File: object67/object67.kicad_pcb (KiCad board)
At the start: 2 copper layers, 200 parts, among them IC1 AK4493SEQ, IC2 TAA5242IRGER, IC3 LMK1C1104PWR, IC4 TPA6120A2DWPR, IC5 TPS7A4701RGWT, IC6 TPS7A3301RGWR, J1 SN37A12B, J2 PJ-037A, J3 Power In, J4 216700-0249, J5 216700-0249, J6 Conn_02x08_Odd_Even, U1 RCJ-2223, U10 ADP5070AREZ, U11 TPS62912, U2 OPA1612AxD, U3 OPA1612AxD, U4 OPA1612AxD, U5 RCJ-2223, U6 OPA1612AxD, U7 TPS7A2050PDQNR, U8 TPS7A2033PDQNR, U9 TPS7A2033PDQNR, Y3 ASDLJ-E-49.152MHZ-L-R-T, Y4 ASDLJ-E-45.1584MHz-L-R-T

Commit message: Updated pcb
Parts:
- added R46: 22, Capacitor_SMD:C_0201_0603Metric, F.Cu at (66.9, 97.0)
- moved C76 124.3 mm to (56.6, 142.1)
- moved C77 124.3 mm to (56.6, 144.6)
- moved C85 124.3 mm to (63.4, 159.9)
- moved C86 124.3 mm to (63.4, 162.9)
- moved C87 124.3 mm to (63.4, 165.9)
- moved FB4 124.3 mm to (56.6, 147.1)
- moved IC5 124.3 mm to (62.3, 144.5)
- moved IC6 124.3 mm to (62.3, 151.8)
- moved J4 124.3 mm to (41.3, 168.5)
- moved J5 124.3 mm to (41.3, 173.7)
- moved R41 124.3 mm to (56.6, 149.6)
- moved C59 124.3 mm to (48.6, 142.1)
- moved C60 124.3 mm to (48.6, 144.6)
- moved C61 124.3 mm to (48.6, 147.1)
- moved C62 124.3 mm to (48.6, 149.6)
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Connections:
- C1 pad 2: GNDA -> GND
- C10 pad 2: GNDA -> GND
- C11 pad 2: GNDA -> GND
- C12 pad 2: GNDA -> GND
- C13 pad 2: GNDA -> GND
- C14 pad 2: GNDA -> GND
- C15 pad 2: GNDA -> GND
- C16 pad 2: GNDA -> GND
- C17 pad 2: GNDA -> GND
- C18 pad 2: GNDA -> GND
- C19 pad 2: GNDA -> GND
- C2 pad 2: GNDA -> GND
- C20 pad 2: GNDA -> GND
- C21 pad 2: GNDA -> GND
- C22 pad 1: GNDA -> GND
- C24 pad 2: GNDA -> GND
- C25 pad 2: GNDA -> GND
- C26 pad 2: GNDA -> GND
- C27 pad 2: GNDA -> GND
- C28 pad 1: GNDA -> GND
- C29 pad 1: GNDA -> GND
- C3 pad 2: GNDA -> GND
- C30 pad 2: GNDA -> GND
- C31 pad 2: GNDA -> GND
- C32 pad 1: GNDA -> GND
- C33 pad 1: GNDA -> GND
- C34 pad 2: GNDA -> GND
- C36 pad 2: GNDA -> GND
- C38 pad 2: GNDA -> GND
- C4 pad 2: GNDA -> GND
- C40 pad 2: GNDA -> GND
- C42 pad 2: GNDA -> GND
- C43 pad 1: GNDA -> GND
- C44 pad 2: GNDA -> GND
- C45 pad 1: GNDA -> GND
- C46 pad 2: GNDA -> GND
- C47 pad 1: GNDA -> GND
- C48 pad 2: GNDA -> GND
- C49 pad 1: GNDA -> GND
- C5 pad 2: GNDA -> GND
- C50 pad 2: GNDA -> GND
- C51 pad 1: GNDA -> GND
- C52 pad 2: GNDA -> GND
- C53 pad 1: GNDA -> GND
- C54 pad 1: GNDA -> GND
- C55 pad 1: GNDA -> GND
- C56 pad 1: GNDA -> GND
- C57 pad 1: GNDA -> GND
- C59 pad 2: GNDA -> GND
- C6 pad 2: GNDA -> GND
- C60 pad 2: GNDA -> GND
- C61 pad 2: GNDA -> GND
- C62 pad 2: GNDA -> GND
- C63 pad 2: GNDA -> GND
- C64 pad 2: GNDA -> GND
- C65 pad 2: GNDA -> GND
- C66 pad 2: GNDA -> GND
- C67 pad 2: GNDA -> GND
- C68 pad 2: GNDA -> GND
- C69 pad 2: GNDA -> GND
- C7 pad 2: GNDA -> GND
- C70 pad 2: GNDA -> GND
- C71 pad 1: GNDA -> GND
- C72 pad 1: GNDPWR -> GND
- C73 pad 1: GNDA -> GND
- C74 pad 1: GNDA -> GND
- C75 pad 2: GNDA -> GND
- C76 pad 1: GNDPWR -> GND
- C77 pad 1: GNDPWR -> GND
- C78 pad 1: GNDPWR -> GND
- C79 pad 1: GNDPWR -> GND
- C8 pad 2: GNDA -> GND
- C80 pad 1: GNDPWR -> GND
- C81 pad 1: GNDPWR -> GND
- C82 pad 1: GNDPWR -> GND
- C83 pad 1: GNDPWR -> GND
- C84 pad 1: GNDPWR -> GND
- C85 pad 1: GNDPWR -> GND
- C86 pad 1: GNDPWR -> GND
- C87 pad 1: GNDA -> GND
- C88 pad 2: GNDA -> GND
- C89 pad 2: GNDA -> GND
- C9 pad 2: GNDA -> GND
- C90 pad 2: GNDA -> GND
- C92 pad 1: GNDA -> GND
- C93 pad 2: GNDA -> GND
- C94 pad 2: GNDA -> GND
- C95 pad 2: GNDA -> GND
- C96 pad 2: GNDA -> GND
- C97 pad 2: GNDA -> GND
- H1 pad 1: GNDPWR -> GND
- IC1 pad 12: GNDA -> GND
- IC1 pad 13: GNDA -> GND
- IC1 pad 17: GNDA -> GND
- IC1 pad 18: GNDA -> GND
- IC1 pad 21: GNDA -> GND
- IC1 pad 22: GNDA -> GND
- IC1 pad 24: GNDA -> GND
- IC1 pad 27: GNDA -> GND
- IC1 pad 28: GNDA -> GND
- IC1 pad 31: GNDA -> GND
- IC1 pad 32: GNDA -> GND
- IC1 pad 37: GNDA -> GND
- IC1 pad 39: GNDA -> GND
- IC1 pad 40: GNDA -> GND
- IC1 pad 43: GNDA -> GND
- IC1 pad 45: GNDA -> GND
- IC1 pad 46: MLCK_{DAC} -> Net-(IC1-MCLK)
- IC1 pad 47: GNDA -> GND
- IC2 pad 13: GNDA -> GND
- IC2 pad 19: GNDA -> GND
- IC2 pad 20: GNDA -> GND
- IC2 pad 21: GNDA -> GND
- IC2 pad 22: GNDA -> GND
- IC2 pad 25: GNDA -> GND
- IC2 pad 26: GNDA -> GND
- IC2 pad 27: GNDA -> GND
- IC2 pad 28: GNDA -> GND
- IC2 pad 29: GNDA -> GND
- IC2 pad 5: GNDA -> GND
- IC2 pad 7: GNDA -> GND
- IC2 pad 8: GNDA -> GND
- IC2 pad 9: GNDA -> GND
- IC3 pad 4: GNDA -> GND
- IC4 pad 21: GNDA -> GND
- IC5 pad 21: GNDA -> GND
- IC5 pad 4: GNDA -> GND
- IC5 pad 5: GNDA -> GND
- IC5 pad 7: GNDA -> GND
- IC5 pad 9: GNDA -> GND
- J1 pad S: GNDA -> GND
- J2 pad 1: GNDPWR -> GND
- J3 pad 2: GNDPWR -> GND
- J4 pad 10: GNDA -> GND
- J4 pad 11: GNDA -> GND
- J4 pad 12: GNDA -> GND
- J4 pad 13: GNDA -> GND
- J4 pad 14: GNDA -> GND
- J4 pad 15: GNDA -> GND
- J4 pad 21: GNDA -> GND
- J4 pad 22: GNDA -> GND
- J4 pad 23: GNDA -> GND
- J4 pad 24: GNDA -> GND
- J5 pad 10: GNDA -> GND
- J5 pad 11: GNDA -> GND
- J5 pad 12: GNDA -> GND
- J5 pad 13: GNDA -> GND
- J5 pad 14: GNDA -> GND
- J5 pad 15: GNDA -> GND
- J5 pad 21: GNDA -> GND
- J5 pad 22: GNDA -> GND
- J5 pad 23: GNDA -> GND
- J5 pad 24: GNDA -> GND
- J5 pad 7: GNDA -> GND
- J5 pad 8: GNDA -> GND
- J5 pad 9: GNDA -> GND
- J6 pad 15: GNDA -> GND
- L2 pad 1: GNDPWR -> GND
- R25 pad 1: GNDA -> GND
- R27 pad 1: GNDA -> GND
- R33 pad 1: GNDA -> GND
- R34 pad 1: GNDA -> GND
- R38 pad 1: GNDA -> GND
- R41 pad 1: GNDPWR -> GND
- R43 pad 1: GNDPWR -> GND
- R45 pad 1: GNDA -> GND
- R6 pad 1: GNDA -> GND
- R7 pad 1: GNDA -> GND
- U10 pad 1: GNDPWR -> GND
- U10 pad 15: GNDA -> GND
- U10 pad 21: GNDA -> GND
- U10 pad 4: GNDA -> GND
- U11 pad 4: GNDPWR -> GND
- U11 pad 7: GNDPWR -> GND
- U4 pad 3: GNDA -> GND
- U4 pad 5: GNDA -> GND
- U6 pad 3: GNDA -> GND
- U6 pad 5: GNDA -> GND
- U7 pad 2: GNDA -> GND
- U7 pad 5: GNDA -> GND
- U8 pad 2: GNDA -> GND
- U8 pad 5: GNDA -> GND
- U9 pad 2: GNDA -> GND
- U9 pad 5: GNDA -> GND
- Y3 pad 2: GNDA -> GND
- Y4 pad 2: GNDA -> GND
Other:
- copper layers 2 -> 4

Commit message: More layouts
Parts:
- moved J1 278.7 mm to (303.5, 150.2)
- moved U1 260.2 mm to (302.8, 129.5), turned to -90 degrees
- moved U5 259.3 mm to (303.0, 109.3), turned to -90 degrees
- moved IC4 233.7 mm to (275.5, 150.5)
- moved IC2 227.9 mm to (257.3, 146.7)
- moved U6 225.4 mm to (273.5, 136.3), turned to 90 degrees
- moved U4 224.6 mm to (273.3, 130.1), turned to 90 degrees
- moved U3 224.0 mm to (273.1, 123.8), turned to 90 degrees
- moved U2 223.3 mm to (273.3, 116.6), turned to 90 degrees
- moved IC5 213.4 mm to (272.4, 107.3)
- moved IC6 202.5 mm to (259.9, 107.3)
- moved IC1 202.4 mm to (257.0, 132.3)
- moved J6 200.9 mm to (232.1, 158.0), turned to -90 degrees
- moved IC3 200.0 mm to (244.5, 138.0), turned to 90 degrees
- moved J4 191.0 mm to (229.4, 135.6), turned to 180 degrees
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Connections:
- IC3 pad 3: MLCK_{MCU} -> MLCK_{DAC}
- IC3 pad 8: MLCK_{DAC} -> MLCK_{MCU}
- TP10 pad 1: MLCK_{MCU} -> MLCK_{DAC}
- TP9 pad 1: MLCK_{DAC} -> MLCK_{MCU}

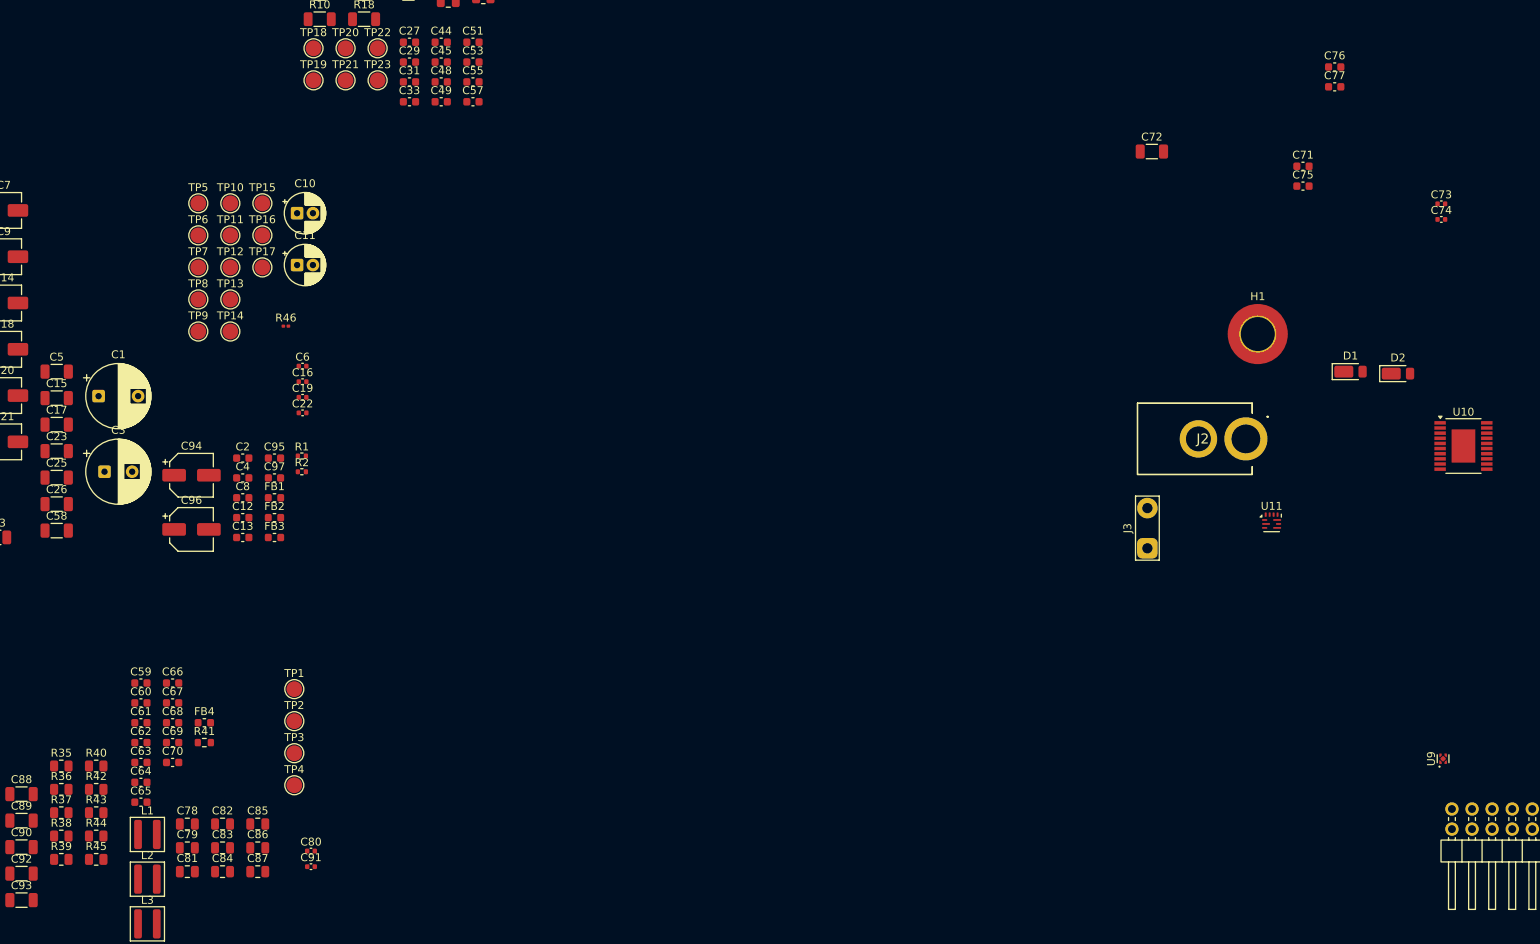
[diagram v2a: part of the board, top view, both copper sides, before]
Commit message: Layout for ADP5070
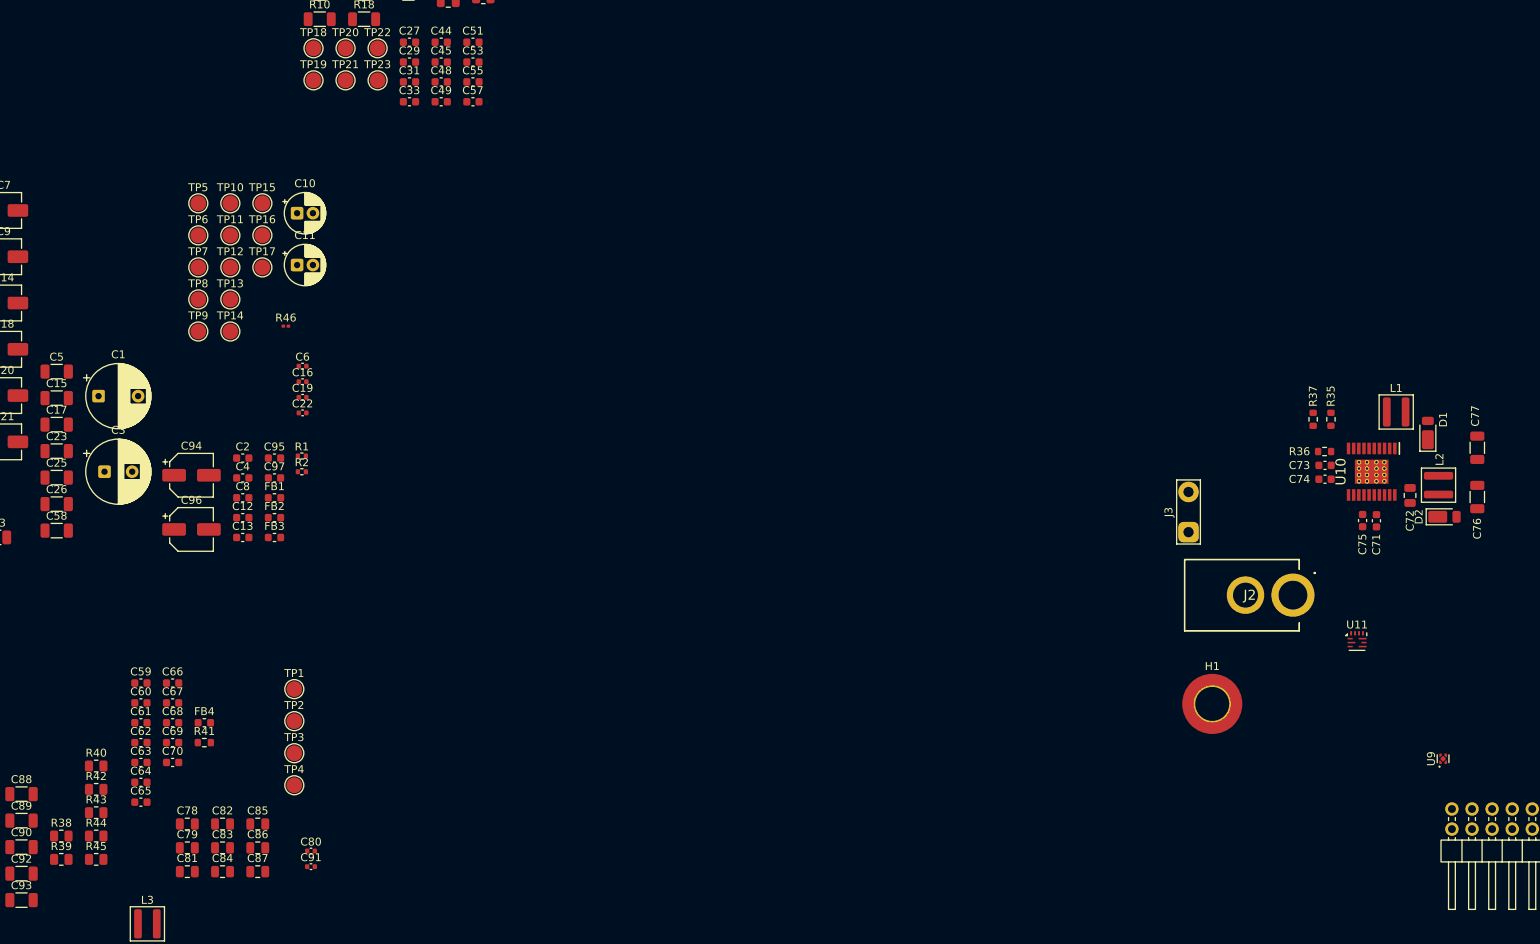
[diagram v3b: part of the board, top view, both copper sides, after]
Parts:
- C72: footprint Capacitor_SMD:C_1206_3216Metric -> Capacitor_SMD:C_0805_2012Metric
- C73, C74: footprint Capacitor_SMD:C_0402_1005Metric -> Capacitor_SMD:C_0603_1608Metric
- C76, C77: footprint Capacitor_SMD:C_0603_1608Metric -> Capacitor_SMD:C_1206_3216Metric
- R35, R36, R37: footprint Resistor_SMD:R_0805_2012Metric -> Resistor_SMD:R_0603_1608Metric
- U10: footprint Package_SO:ETSSOP-20-1EP_4.4x6.5mm_P0.65mm_EP3x4.2mm -> object67:SOP65P640X120-21N
- moved L2 170.6 mm to (212.6, 117.1), turned to -90 degrees
- moved L1 166.6 mm to (207.2, 107.8)
- moved R35 166.4 mm to (199.0, 108.8), turned to -90 degrees
- moved R37 165.9 mm to (196.7, 108.8), turned to -90 degrees
- moved R36 165.3 mm to (198.2, 112.8)
- moved C76 57.3 mm to (217.5, 118.6), turned to -90 degrees
- moved C72 54.4 mm to (209.0, 118.4), turned to -90 degrees
- moved C77 49.1 mm to (217.5, 112.4), turned to 90 degrees
- moved H1 47.1 mm to (184.0, 144.8)
- moved C71 45.8 mm to (204.7, 121.6), turned to 90 degrees
- moved C75 42.9 mm to (203.0, 121.6), turned to -90 degrees
- moved C73 36.2 mm to (198.2, 114.6), turned to 180 degrees
- moved C74 36.0 mm to (198.2, 116.3)
- moved J2 20.6 mm to (194.2, 131.0)
- moved D2 19.0 mm to (213.3, 121.1)
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
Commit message: Finished layout for ADC DAC, starting filter
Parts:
- removed FB3: 600R, Inductor_SMD:L_0603_1608Metric
- removed TP1, TP11, TP12, TP13, TP14, TP15, TP16, TP17, TP2: TestPoint, TestPoint:TestPoint_Pad_D2.0mm
- added C98: 10u, Capacitor_SMD:CP_Elec_4x5.3, F.Cu at (284.5, 56.0)
- added C99: 0.1u, Capacitor_SMD:C_0603_1608Metric, F.Cu at (282.0, 62.8)
- C23: value 0.1u -> 10u
- C5: value 1u -> 10u; footprint Capacitor_SMD:C_1206_3216Metric -> Capacitor_SMD:CP_Elec_4x5.3
- C6: footprint Capacitor_SMD:C_0402_1005Metric -> Capacitor_SMD:C_0603_1608Metric
- R42, R43: footprint Resistor_SMD:R_0805_2012Metric -> Resistor_SMD:R_0603_1608Metric
- TP10, TP18, TP19, TP20, TP21, TP22, TP23, TP3, TP4, TP5, TP6, TP7, TP8, TP9: footprint TestPoint:TestPoint_Pad_D2.0mm -> TestPoint:TestPoint_Pad_D1.0mm
- moved C58 261.8 mm to (292.8, 63.0)
- moved C25 259.8 mm to (292.8, 65.5)
- moved C26 259.5 mm to (292.8, 70.5)
- moved C23 258.7 mm to (292.8, 68.0), turned to 180 degrees
- moved C20 253.0 mm to (279.2, 56.0), turned to 90 degrees
- moved C9 251.3 mm to (282.5, 89.0)
- moved C1 250.2 mm to (293.0, 92.0), turned to 135 degrees
- moved C94 248.9 mm to (303.5, 101.5), turned to 90 degrees
- moved C96 248.8 mm to (303.5, 111.2), turned to -90 degrees
- moved C21 245.9 mm to (272.2, 62.8), turned to 90 degrees
- moved C5 244.3 mm to (280.7, 75.0), turned to 180 degrees
- moved C7 240.2 mm to (270.9, 97.7), turned to 180 degrees
- moved C18 239.6 mm to (270.9, 102.9), turned to 180 degrees
- moved C14 238.9 mm to (270.2, 92.4)
- moved C3 237.6 mm to (281.5, 121.2)
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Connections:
- C14 pad 1: Net-(Y4-VDD) -> VFiltered
- C16 pad 1: Net-(Y4-VDD) -> VFiltered
- C18 pad 1: Net-(Y3-VDD) -> Net-(IC1-DVDD)
- C19 pad 1: Net-(Y3-VDD) -> VFiltered
- C63 pad 1: +5VA -> +5.39574468085V
- C64 pad 1: +5VA -> +5.39574468085V
- C67 pad 1: +5VP -> +5.39574468085V
- C68 pad 1: +5VP -> +5.39574468085V
- FB1 pad 1: Net-(Y4-VDD) -> VFiltered
- IC1 pad 1: +3.3V -> Net-(IC1-DVDD)
- U8 pad 3: +5VA -> +5.39574468085V
- U8 pad 4: +5VA -> +5.39574468085V
- U9 pad 3: +5VP -> +5.39574468085V
- U9 pad 4: +5VP -> +5.39574468085V
- Y3 pad 4: Net-(Y3-VDD) -> VFiltered
- Y4 pad 4: Net-(Y4-VDD) -> VFiltered

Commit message: Filter
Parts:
- J6: footprint Connector_PinHeader_2.54mm:PinHeader_2x08_P2.54mm_Horizontal -> Connector_PinHeader_2.54mm:PinHeader_2x08_P2.54mm_Vertical
- moved C28 302.2 mm to (304.9, 189.8)
- moved C24 296.3 mm to (304.9, 171.5)
- moved C32 281.6 mm to (304.2, 155.2)
- moved C30 277.8 mm to (304.4, 137.0)
- moved C43 267.7 mm to (277.5, 187.5)
- moved C42 262.0 mm to (277.0, 171.2)
- moved C47 246.9 mm to (276.2, 155.2)
- moved C46 239.6 mm to (276.2, 132.5)
- moved J6 106.2 mm to (182.3, 161.2), turned to 180 degrees
- moved U6 88.9 mm to (277.3, 179.9)
- moved U3 78.3 mm to (304.3, 180.2)
- moved C20 72.1 mm to (240.1, 116.6)
- moved C21 72.1 mm to (233.1, 123.3)
- moved C22 72.1 mm to (238.3, 125.6)
- moved C25 72.1 mm to (253.6, 126.1)
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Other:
- board outline added: 220 x 92 mm

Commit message: Filter
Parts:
- moved C90 265.6 mm to (296.3, 125.0), turned to 90 degrees
- moved C88 265.4 mm to (296.3, 119.5), turned to -90 degrees
- moved C92 255.7 mm to (284.4, 116.7), turned to -90 degrees
- moved C89 251.0 mm to (280.6, 115.4)
- moved C93 249.3 mm to (278.4, 122.9), turned to 90 degrees
- moved R45 246.2 mm to (286.4, 128.4), turned to 180 degrees
- moved C87 243.2 mm to (301.8, 118.2), turned to 180 degrees
- moved R44 241.9 mm to (282.6, 128.4), turned to 180 degrees
- moved R13 230.4 mm to (277.2, 155.2)
- moved R12 227.5 mm to (274.2, 151.2), turned to 90 degrees
- moved R11 226.6 mm to (270.5, 152.5)
- moved C39 224.7 mm to (291.3, 144.5)
- moved R19 224.5 mm to (281.8, 138.2)
- moved C35 221.7 mm to (277.8, 151.5)
- moved R18 217.8 mm to (277.8, 142.2)
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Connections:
- C35 pad 1: Net-(U4A--) -> Net-(U4B--)
- C39 pad 1: Net-(U4B--) -> Net-(U4A--)
- IC6 pad 21: unconnected-(IC6-GND_2-Pad21) -> GND
- IC6 pad 7: unconnected-(IC6-GND_1-Pad7) -> GND
- R12 pad 2: Net-(U4A--) -> Net-(U4B--)
- R18 pad 2: Net-(U4B--) -> Net-(U4A--)
- U4 pad 1: AOUTLP2 -> AOUTLN2
- U4 pad 7: AOUTLN2 -> AOUTLP2

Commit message: Finished layout, start MCU
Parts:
- removed C52, C54: 10u, Capacitor_SMD:CP_Elec_4x5.3
- removed TP18, TP19, TP9: TestPoint, TestPoint:TestPoint_Pad_D1.0mm
- removed U2, U3, U4, U6: OPA1612AxD, Package_SON:WSON-8-1EP_3x3mm_P0.5mm_EP1.2x2mm_ThermalVias
- added IC10: OPA1612AIDRGR, Package_SON:WSON-8-1EP_3x3mm_P0.5mm_EP1.2x2mm_ThermalVias, F.Cu at (272.4, 149.1)
- added IC7: OPA1612AIDRGR, Package_SON:WSON-8-1EP_3x3mm_P0.5mm_EP1.2x2mm_ThermalVias, F.Cu at (301.5, 134.7)
- added IC8: OPA1612AIDRGR, Package_SON:WSON-8-1EP_3x3mm_P0.5mm_EP1.2x2mm_ThermalVias, F.Cu at (302.0, 146.1)
- added IC9: OPA1612AIDRGR, Package_SON:WSON-8-1EP_3x3mm_P0.5mm_EP1.2x2mm_ThermalVias, F.Cu at (272.5, 173.9)
- R10, R3, R4, R5, R6, R7, R8, R9: footprint Resistor_SMD:R_1206_3216Metric -> Resistor_SMD:R_0603_1608Metric
- R38, R39, R40: footprint Resistor_SMD:R_0805_2012Metric -> Resistor_SMD:R_0603_1608Metric
- moved R33 298.7 mm to (328.8, 117.0)
- moved C50 288.7 mm to (317.2, 172.5)
- moved C56 279.3 mm to (317.0, 167.5), turned to 180 degrees
- moved R31 277.8 mm to (327.3, 179.4), turned to 180 degrees
- moved R34 270.5 mm to (328.8, 166.4)
- moved R32 269.4 mm to (319.6, 179.4)
- moved R23 255.1 mm to (300.7, 181.2), turned to 180 degrees
- moved FILOUTRP 254.7 mm to (300.0, 184.2)
- moved R25 254.6 mm to (304.2, 181.2), turned to 180 degrees
- moved R3 253.2 mm to (304.2, 134.1), turned to -90 degrees
- moved R7 253.0 mm to (301.7, 152.5), turned to 90 degrees
- moved R24 251.6 mm to (301.2, 177.2), turned to 180 degrees
- moved R8 251.5 mm to (302.5, 150.2)
- moved R26 251.1 mm to (303.2, 179.2)
- moved R9 250.8 mm to (304.7, 146.2), turned to 90 degrees
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- renumbered TP3 to +16, TP4 to -16, TP22 to FILOUTLN, TP23 to FILOUTRN, TP21 to FILOUTRP, TP20 to TPFILOUTLP, TP6 to TPLN, TP5 to TPLP, TP10 to TPMCLK, TP7 to TPRN, TP8 to TPRP
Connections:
- net Net-(R3-Pad1) renamed OPA14
- net Net-(R8-Pad2) renamed OPA20
- net Net-(U2A--) renamed OPA12
- net Net-(U2B--) renamed OPA15
- net Net-(U3A--) renamed OPA18
- net Net-(U3B--) renamed OPA21
- net Net-(U4A--) renamed OPA9
- net Net-(U4B--) renamed OPA6
- net Net-(U6A--) renamed OPA0
- net Net-(U6B--) renamed OPA3
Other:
- board size 220 x 92 mm -> 198.2 x 92 mm
